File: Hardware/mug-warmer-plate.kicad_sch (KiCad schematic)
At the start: 7 parts

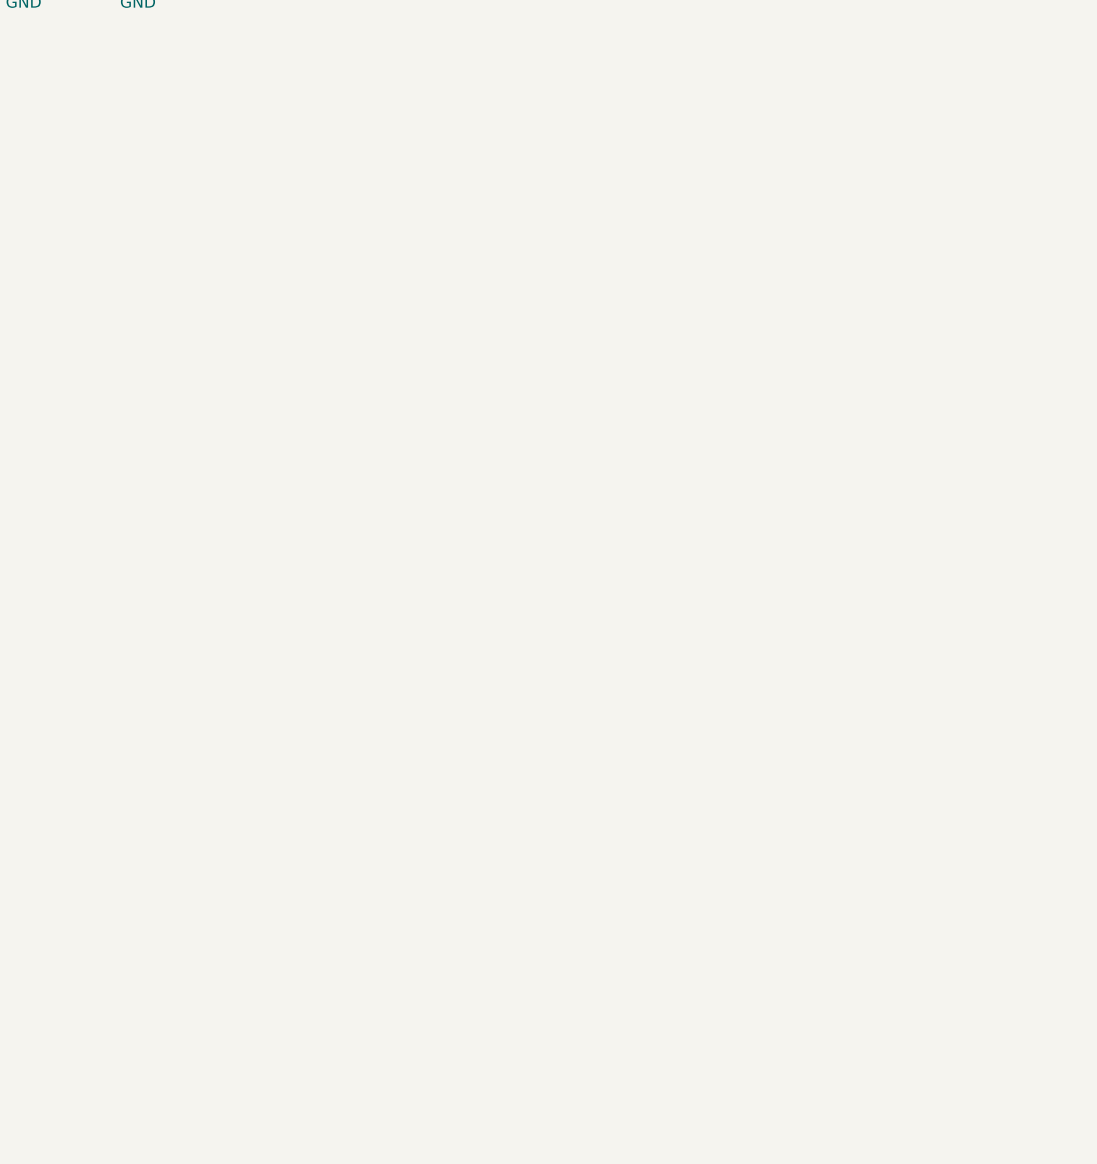
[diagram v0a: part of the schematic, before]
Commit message: Added microprocessor block
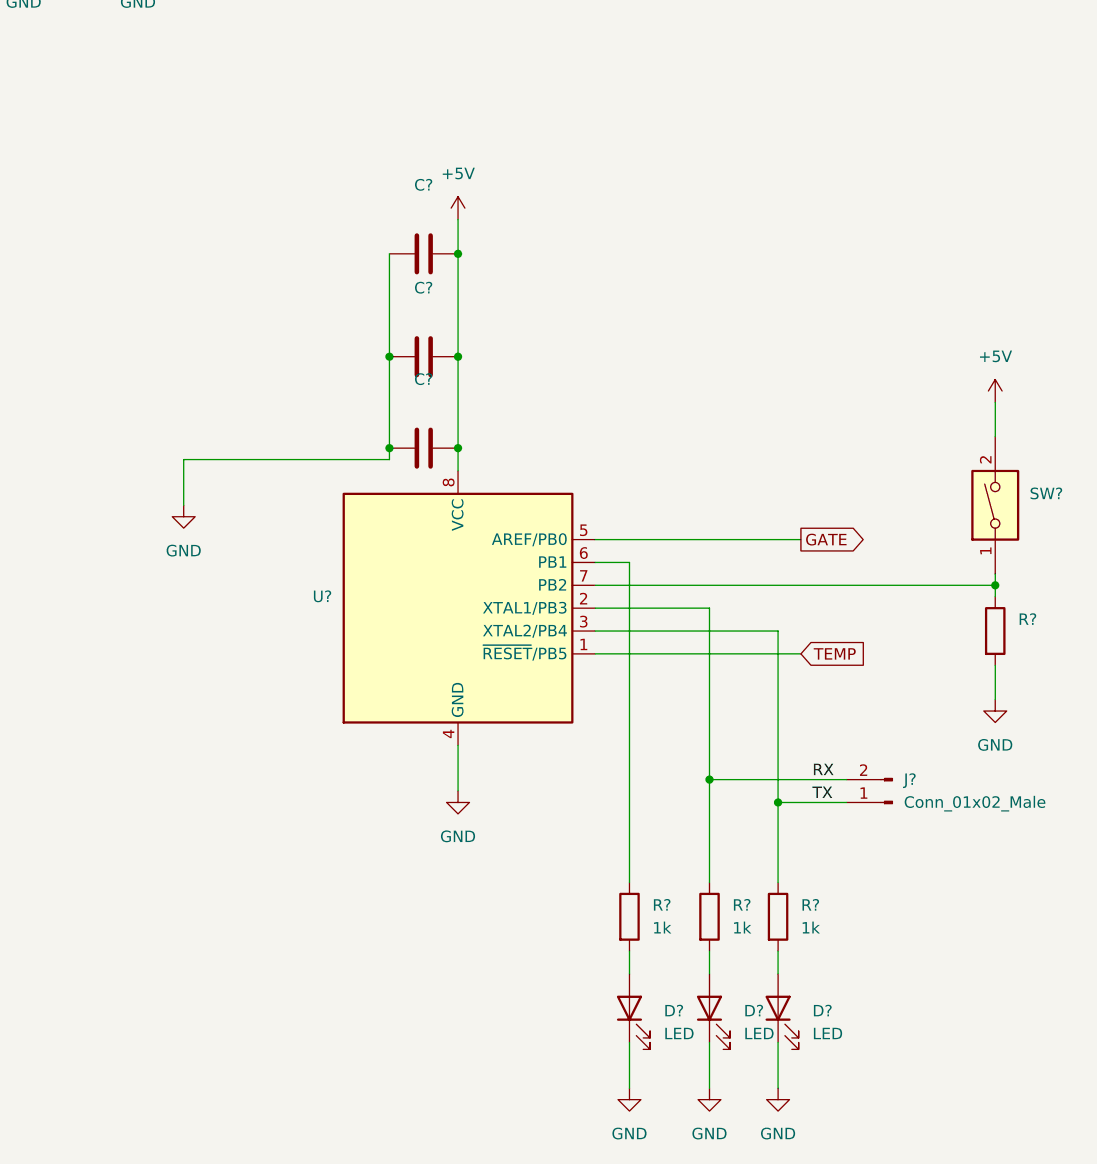
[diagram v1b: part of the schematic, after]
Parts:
- added C? (x3): (no value), symbol Device:C
- added D? (x3): LED, symbol Device:LED
- added J?: Conn_01x02_Male, symbol Connector:Conn_01x02_Male
- added R? (x3): 1k, symbol Device:R
- added R?: (no value), symbol Device:R
- added SW?: (no value), symbol Switch:SW_DIP_x01
- added U?: (no value), symbol MCU_Microchip_ATtiny:ATtiny85-20P
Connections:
- net +5V: now also C?.2, C?.2, C?.2, SW?.2, U?.8 (VCC)
- net GND: now also C?.1, C?.1, C?.1, D?.1 (K), D?.1 (K), D?.1 (K), R?.2, U?.4 (GND)
- new net: R?.1, U?.6 (PB1)
- new net: R?.1, SW?.1, U?.7 (PB2)
- new net: D?.2 (A), R?.2 (x3)
- new net GATE: U?.5 (AREF/PB0)
- new net RX: J?.2 (Pin_2), R?.1, U?.2 (XTAL1/PB3)
- new net TEMP: U?.1 (~{RESET}/PB5)
- new net TX: J?.1 (Pin_1), R?.1, U?.3 (XTAL2/PB4)

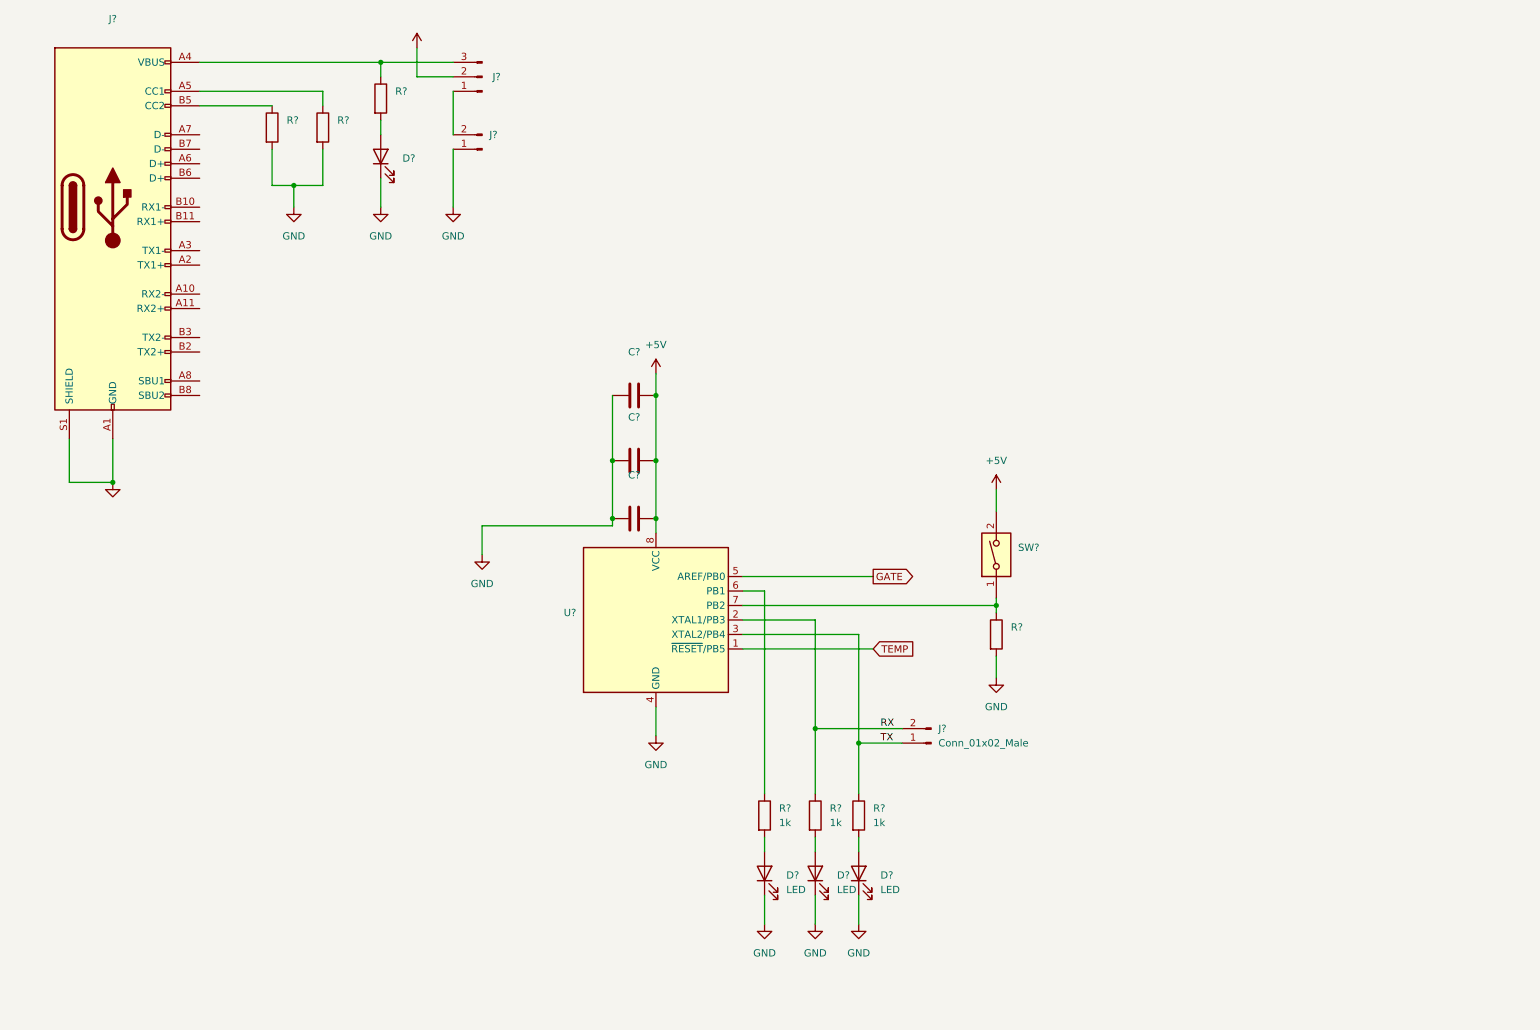
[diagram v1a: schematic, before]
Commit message: Completed circuit schematic
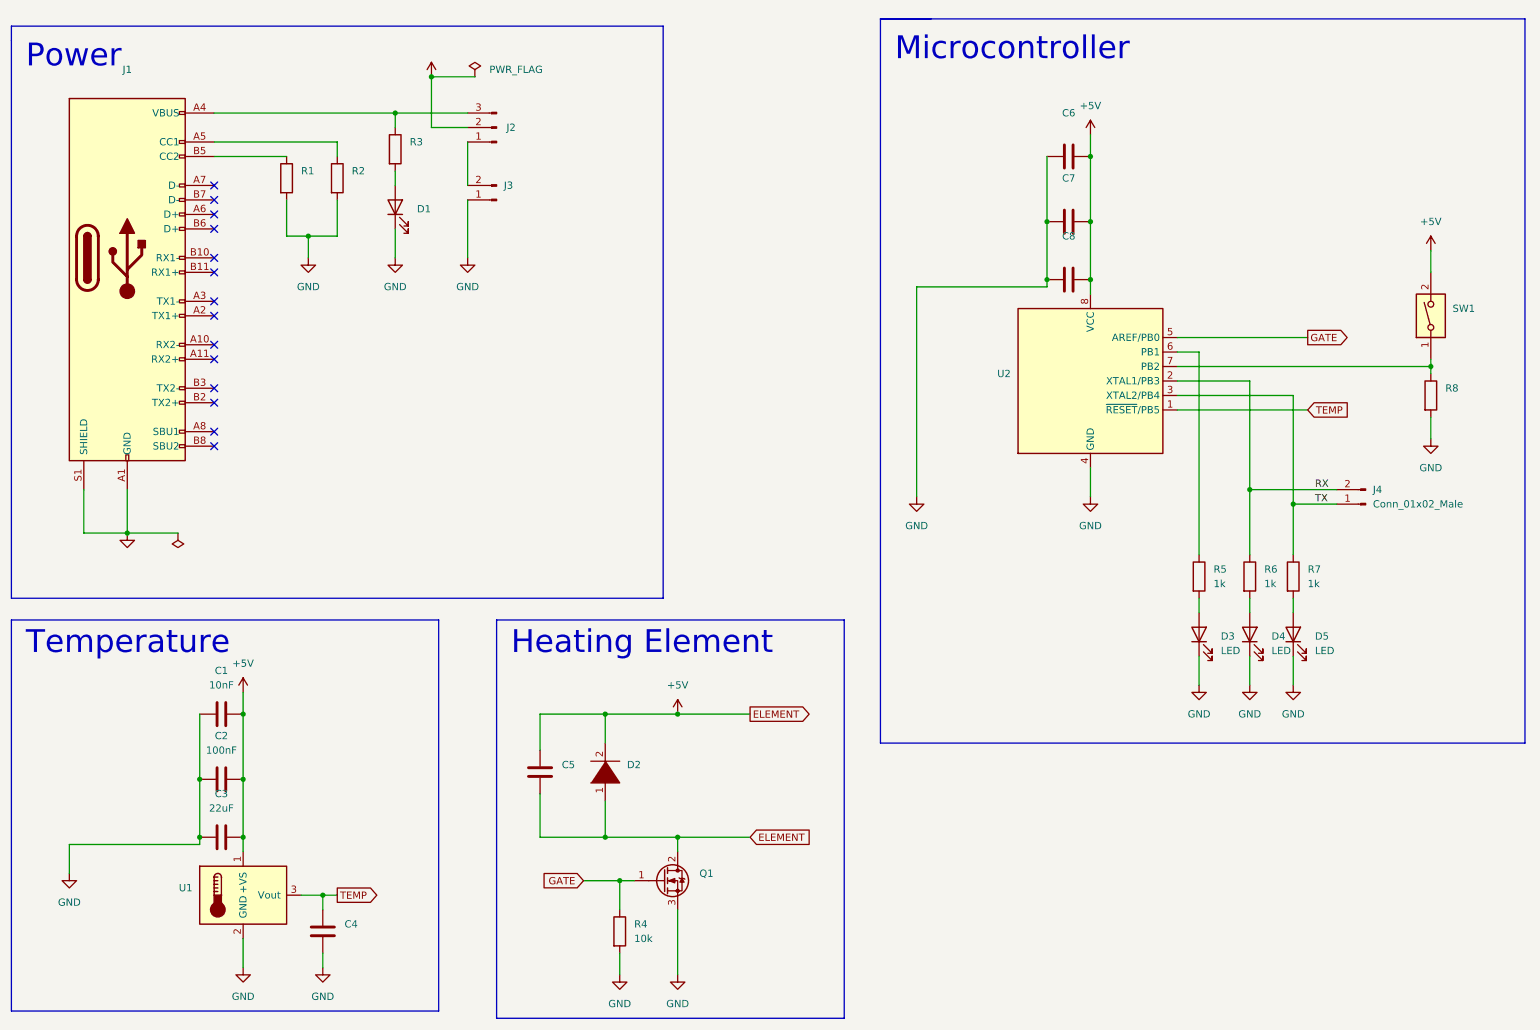
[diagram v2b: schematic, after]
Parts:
- added C1: 10nF, symbol Device:C
- added C2: 100nF, symbol Device:C
- added C3: 22uF, symbol Device:C
- added C4, C5: (no value), symbol Device:C
- added D2: (no value), symbol pspice:DIODE
- added Q1: (no value), symbol Transistor_FET:IRLZ44N
- added R4: 10k, symbol Device:R
- added U1: (no value), symbol Sensor_Temperature:LM35-NEB
- gave numbers to parts that had none: 20
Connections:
- net +5V: now also C1.2, C2.2, C3.2, C5.1, C5.2, D2.1 (K), D2.2 (A), Q1.2 (D), U1.1 (+VS)
- net GATE: now also Q1.1 (G), R4.1
- net GND: now also C1.1, C2.1, C3.1, C4.1, Q1.3 (S), R4.2, U1.2 (GND)
- net TEMP: now also C4.2, U1.3 (Vout)
- no-connect marks 0 -> 14
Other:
- note added: "Heating Element"
- note added: "Microcontroller"
- note added: "Power"
- note added: "Temperature"
- moved on the sheet: C6, C7, C8, D1, D3, D4, D5, J1, J2, J3, J4, R1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

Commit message: Replaced 5V pin with testpad
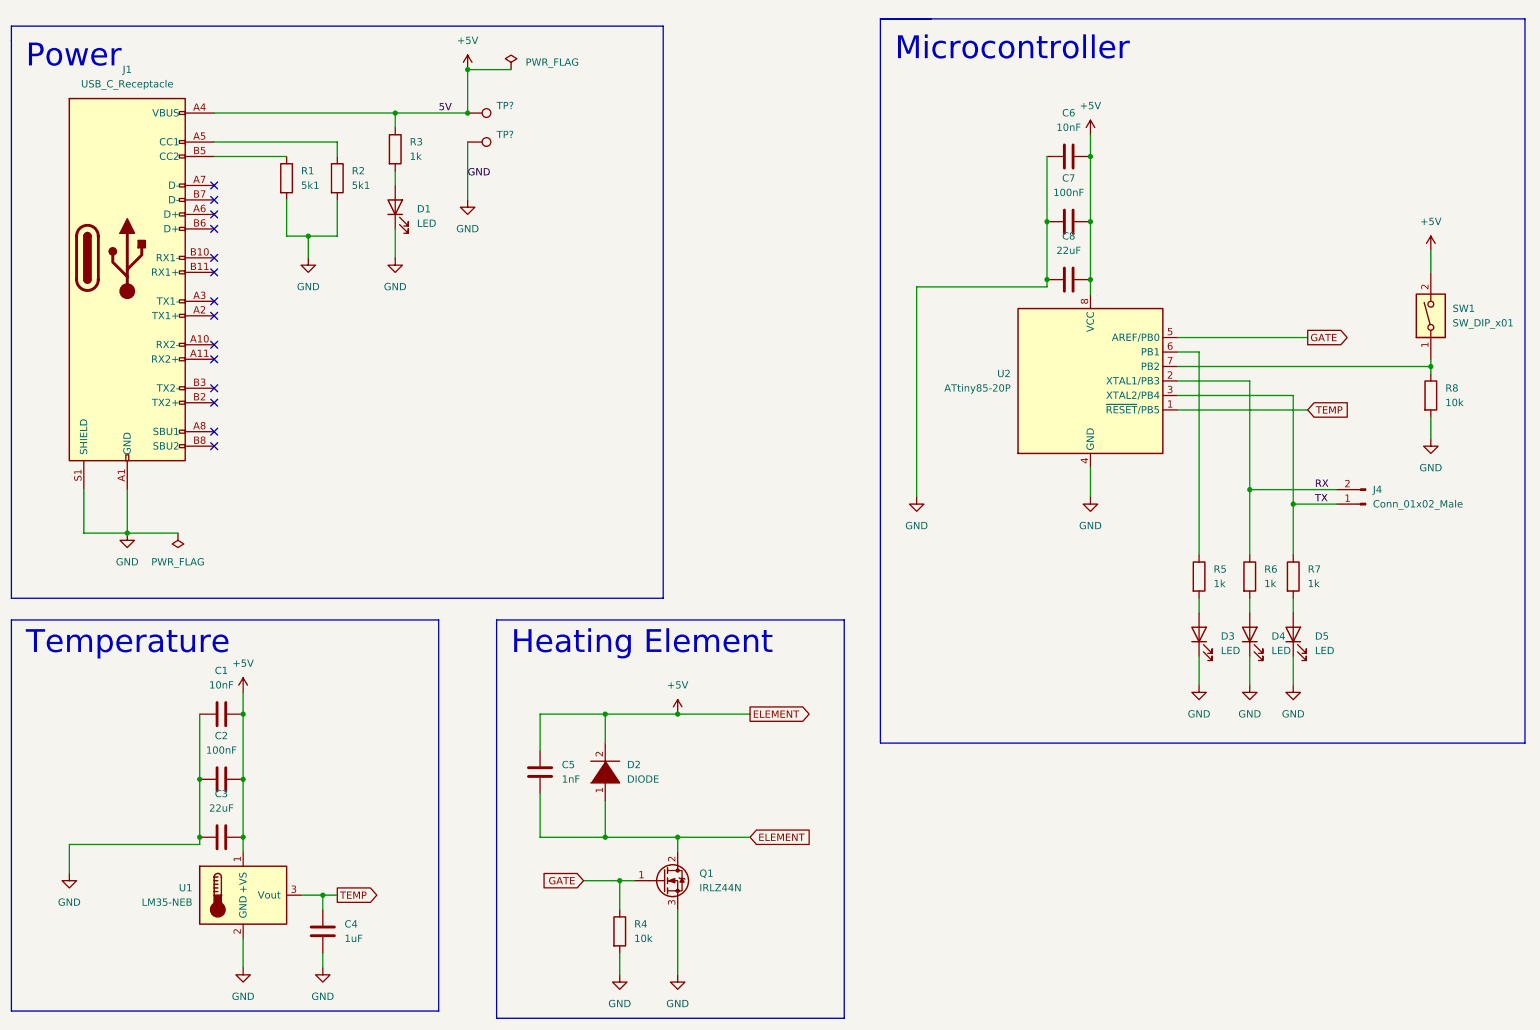
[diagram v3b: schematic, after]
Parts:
- removed J2: (no value), symbol Connector:Conn_01x03_Male
- removed J3: (no value), symbol Connector:Conn_01x02_Male
- added TP? (x2): (no value), symbol Connector:TestPoint
- C4: value (none) -> 1uF
- C5: value (none) -> 1nF
- C6: value (none) -> 10nF
- C7: value (none) -> 100nF
- C8: value (none) -> 22uF
- D1: value (none) -> LED
- D2: value (none) -> DIODE
- J1: value (none) -> USB_C_Receptacle
- Q1: value (none) -> IRLZ44N; footprint (none) -> Package_TO_SOT_THT:TO-220-3_Vertical
- R1, R2: value (none) -> 5k1
- R3: value (none) -> 1k
- R8: value (none) -> 10k
- SW1: value (none) -> SW_DIP_x01
- U1: value (none) -> LM35-NEB
- U2: value (none) -> ATtiny85-20P; footprint (none) -> Package_DIP:DIP-8_W7.62mm
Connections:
- net +5V: now also J1.A4 (VBUS), J1.A9 (VBUS), J1.B4 (VBUS), J1.B9 (VBUS), R3.1, TP?.1
- net GND: now also TP?.1

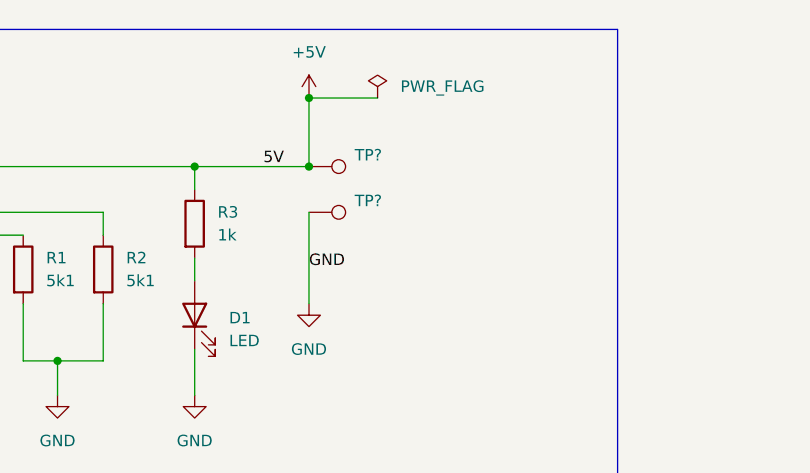
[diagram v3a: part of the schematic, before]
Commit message: Defined all component footprint
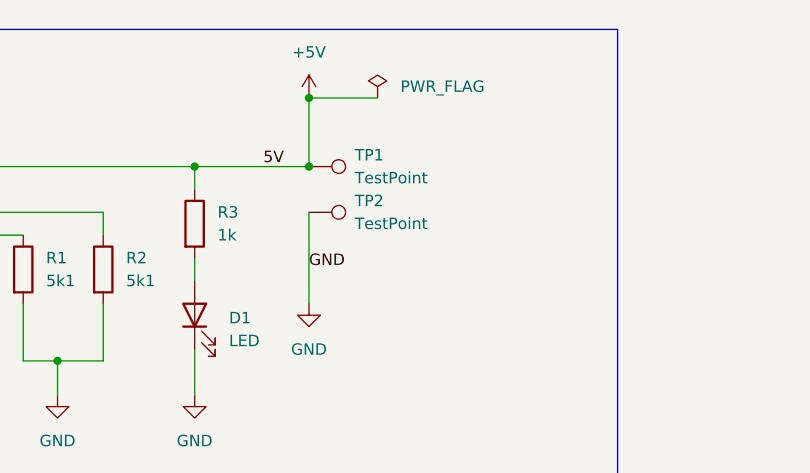
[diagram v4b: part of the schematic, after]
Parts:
- C1, C2, C5, C6, C7: footprint (none) -> Capacitor_THT:C_Disc_D4.3mm_W1.9mm_P5.00mm
- C3, C4, C8: footprint (none) -> Capacitor_THT:C_Radial_D10.0mm_H12.5mm_P5.00mm
- D1, D3, D4, D5: footprint (none) -> LED_THT:LED_D5.0mm
- D2: footprint (none) -> Diode_THT:D_DO-41_SOD81_P7.62mm_Horizontal
- TP1, TP2: renamed from TP?; value (none) -> TestPoint
